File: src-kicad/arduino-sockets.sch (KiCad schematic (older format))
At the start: 48 parts, among them J10 1x8_female_pin_Header_2.54mm, J11 1x6_female_pin_Header_2.54mm, J12 1x6_male_pin_Header_2.54mm, J13 1x6_male_pin_Header_2.54mm, J14 1x6_male_pin_Header_2.54mm, J19 2x4_male_pin_Header_2.54mm, J2 1x6_male_pin_Header_2.54mm, J3 1x6_male_pin_Header_2.54mm, J4 1x10_female_pin_Header_2.54mm, J5 1x8_female_pin_Header_2.54mm, J6 1x6_male_pin_Header_2.54mm, J7 1x8_male_pin_Header_2.54mm, J8 1x8_male_pin_Header_2.54mm, J9 1x8_male_pin_Header_2.54mm, U6 TXB0106, U8 TXS0108, U9 TXB0108

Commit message: Kicad pcb migration: Sockets J10 and J4 added
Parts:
- J10, J5: footprint (none) -> Icezum:1x8_Socket_header_2.54mm
- J4: footprint (none) -> Icezum:1x10_socket-header-2.54mm
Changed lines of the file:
@@
 F 0 "J10" V 9400 2000 60  0000 C CNN
 F 1 "1x8_female_pin_Header_2.54mm" H 9600 850 60  0001 C CNN
-F 2 "" H 9250 1600 60  0000 C CNN
+F 2 "Icezum:1x8_Socket_header_2.54mm" H 9250 1600 60  0001 C CNN
 F 3 "" H 9250 1600 60  0000 C CNN
 	1    9250 1050
@@
 F 0 "J4" V 6200 2150 60  0000 C CNN
 F 1 "1x10_female_pin_Header_2.54mm" H 6220 860 60  0001 C CNN
-F 2 "" H 6050 1600 60  0000 C CNN
+F 2 "Icezum:1x10_socket-header-2.54mm" H 6050 1600 60  0001 C CNN
 F 3 "" H 6050 1600 60  0000 C CNN
 	1    6050 1050
@@
 F 0 "J5" V 5550 6700 60  0000 C CNN
 F 1 "1x8_female_pin_Header_2.54mm" H 5750 5600 60  0001 C CNN
-F 2 "" H 5400 6350 60  0000 C CNN
+F 2 "Icezum:1x8_Socket_header_2.54mm" H 5400 6350 60  0001 C CNN
 F 3 "" H 5400 6350 60  0000 C CNN
 	1    5400 5800
@@
 B8 D2 A5 D0 D0 88 43 83 08 6C BD D2 A5 D0 D0 88 C3 36 11 89 E7 80 EE 2B 5D 12 0D 8D 28 1C 42 E0
 0D 11 99 76 E0 6E E0 E3 2B 5D 22 0D 8D 71 EC 07 1E E7 1B 7C F8 FF 01 FB D1 C8 6E 4C 03 14 F4 00
-00 00 00 49 45 4E 44 AE 42 60 82 08
+00 00 00 49 45 4E 44 AE 42 60 82 65
 EndData
 $EndBitmap
@@
 F3 F0 1D 79 17 0B BC D0 AE 96 03 B8 3F 0C 6D B8 A2 A8 0B 16 2C 58 B0 60 C1 82 05 0B 16 2C 58 B0
 60 C1 82 05 0B 16 2C 58 B0 E0 7F 81 FF 00 64 C5 01 8A 14 5C 86 66 00 00 00 00 49 45 4E 44 AE 42
-60 82 00
+60 82 AB
 EndData
 $EndBitmap

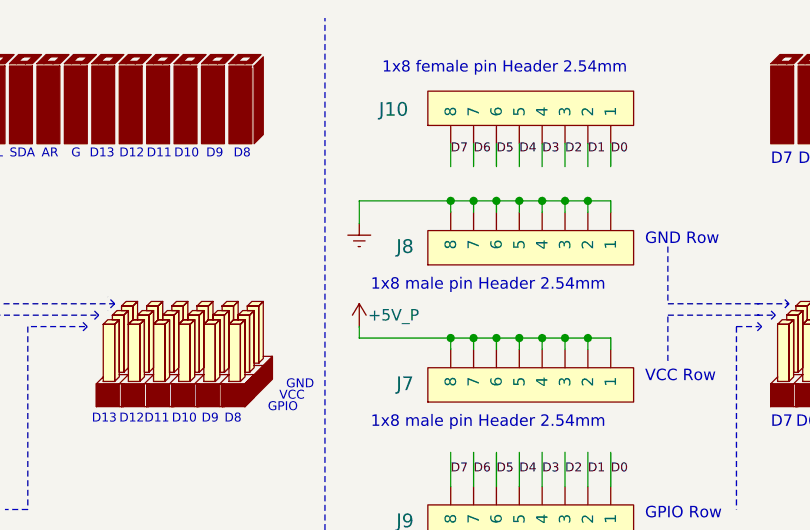
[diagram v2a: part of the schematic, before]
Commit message: Kicad pcb migration: J8 pin header added
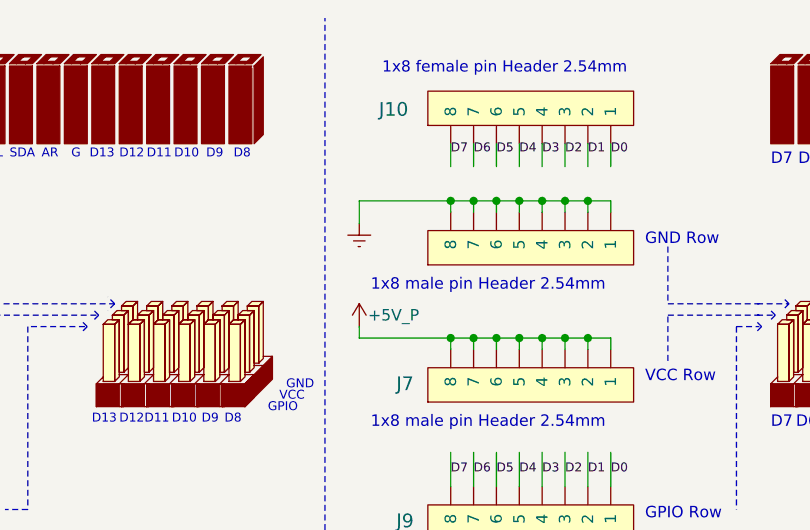
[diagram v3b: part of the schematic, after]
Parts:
- J7, J9: footprint (none) -> Icezum:1x8_Socket_header_2.54mm
- J8: footprint (none) -> Icezum:1x8_pin_header_2.54mm
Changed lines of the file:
@@
 U 1 1 57474AD5
 P 9250 1350
-F 0 "J8" V 9100 2250 60  0000 C CNN
+F 0 "J8" V 9100 2250 60  0001 C CNN
 F 1 "1x8_male_pin_Header_2.54mm" H 9000 1150 60  0001 C CNN
-F 2 "" H 9250 1900 60  0000 C CNN
+F 2 "Icezum:1x8_pin_header_2.54mm" H 9250 1900 60  0001 C CNN
 F 3 "" H 9250 1900 60  0000 C CNN
 	1    9250 1350
@@
 F 0 "J7" V 9100 2850 60  0000 C CNN
 F 1 "1x8_male_pin_Header_2.54mm" H 9140 1760 60  0001 C CNN
-F 2 "" H 9250 2500 60  0000 C CNN
+F 2 "Icezum:1x8_Socket_header_2.54mm" H 9250 2500 60  0001 C CNN
 F 3 "" H 9250 2500 60  0000 C CNN
 	1    9250 1950
@@
 F 0 "J9" V 9100 3450 60  0000 C CNN
 F 1 "1x8_male_pin_Header_2.54mm" H 9140 2360 60  0001 C CNN
-F 2 "" H 9250 3100 60  0000 C CNN
+F 2 "Icezum:1x8_Socket_header_2.54mm" H 9250 3100 60  0001 C CNN
 F 3 "" H 9250 3100 60  0000 C CNN
 	1    9250 2550
@@
 B8 D2 A5 D0 D0 88 43 83 08 6C BD D2 A5 D0 D0 88 C3 36 11 89 E7 80 EE 2B 5D 12 0D 8D 28 1C 42 E0
 0D 11 99 76 E0 6E E0 E3 2B 5D 22 0D 8D 71 EC 07 1E E7 1B 7C F8 FF 01 FB D1 C8 6E 4C 03 14 F4 00
-00 00 00 49 45 4E 44 AE 42 60 82 65
+00 00 00 49 45 4E 44 AE 42 60 82 00
 EndData
 $EndBitmap
@@
 F3 F0 1D 79 17 0B BC D0 AE 96 03 B8 3F 0C 6D B8 A2 A8 0B 16 2C 58 B0 60 C1 82 05 0B 16 2C 58 B0
 60 C1 82 05 0B 16 2C 58 B0 E0 7F 81 FF 00 64 C5 01 8A 14 5C 86 66 00 00 00 00 49 45 4E 44 AE 42
-60 82 AB
+60 82 40
 EndData
 $EndBitmap

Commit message: Kicad pcb migration: Some sockets and header added
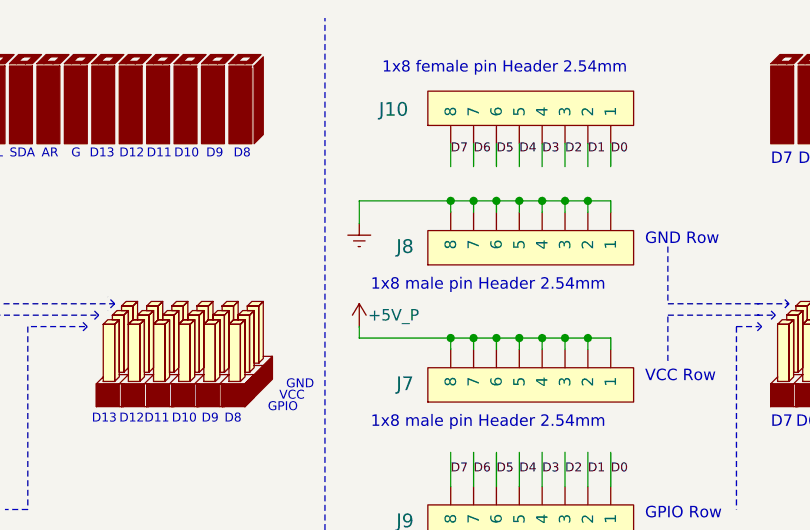
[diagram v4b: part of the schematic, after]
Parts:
- J11: footprint (none) -> Icezum:1x6-Socket-header-2.54mm
- J7, J9: footprint Icezum:1x8_Socket_header_2.54mm -> Icezum:1x8_pin_header_2.54mm
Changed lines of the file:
@@
 U 1 1 57474AD5
 P 9250 1350
-F 0 "J8" V 9100 2250 60  0001 C CNN
+F 0 "J8" V 9100 2250 60  0000 C CNN
 F 1 "1x8_male_pin_Header_2.54mm" H 9000 1150 60  0001 C CNN
 F 2 "Icezum:1x8_pin_header_2.54mm" H 9250 1900 60  0001 C CNN
@@
 F 0 "J7" V 9100 2850 60  0000 C CNN
 F 1 "1x8_male_pin_Header_2.54mm" H 9140 1760 60  0001 C CNN
-F 2 "Icezum:1x8_Socket_header_2.54mm" H 9250 2500 60  0001 C CNN
+F 2 "Icezum:1x8_pin_header_2.54mm" H 9250 2500 60  0001 C CNN
 F 3 "" H 9250 2500 60  0000 C CNN
 	1    9250 1950
@@
 F 0 "J9" V 9100 3450 60  0000 C CNN
 F 1 "1x8_male_pin_Header_2.54mm" H 9140 2360 60  0001 C CNN
-F 2 "Icezum:1x8_Socket_header_2.54mm" H 9250 3100 60  0001 C CNN
+F 2 "Icezum:1x8_pin_header_2.54mm" H 9250 3100 60  0001 C CNN
 F 3 "" H 9250 3100 60  0000 C CNN
 	1    9250 2550
@@
 F 0 "J11" V 8950 5950 60  0000 C CNN
 F 1 "1x6_female_pin_Header_2.54mm" H 8920 5960 60  0001 C CNN
-F 2 "" H 8750 6700 60  0000 C CNN
+F 2 "Icezum:1x6-Socket-header-2.54mm" H 8750 6700 60  0001 C CNN
 F 3 "" H 8750 6700 60  0000 C CNN
 	1    8750 6150
@@
 F3 F0 1D 79 17 0B BC D0 AE 96 03 B8 3F 0C 6D B8 A2 A8 0B 16 2C 58 B0 60 C1 82 05 0B 16 2C 58 B0
 60 C1 82 05 0B 16 2C 58 B0 E0 7F 81 FF 00 64 C5 01 8A 14 5C 86 66 00 00 00 00 49 45 4E 44 AE 42
-60 82 40
+60 82 00
 EndData
 $EndBitmap

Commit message: Kicad pcb migration: I/O pin header connectors placed
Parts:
- J12, J13, J14, J2, J3, J6: footprint (none) -> Icezum:1x6-pin-header-2.54mm
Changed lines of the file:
@@
 F 0 "J3" V 5850 2050 60  0000 C CNN
 F 1 "1x6_male_pin_Header_2.54mm" H 5940 1160 60  0001 C CNN
-F 2 "" H 6050 1900 60  0000 C CNN
+F 2 "Icezum:1x6-pin-header-2.54mm" H 6050 1900 60  0001 C CNN
 F 3 "" H 6050 1900 60  0000 C CNN
 	1    6050 1350
@@
 F 0 "J2" V 5850 2650 60  0000 C CNN
 F 1 "1x6_male_pin_Header_2.54mm" H 5940 1760 60  0001 C CNN
-F 2 "" H 6050 2500 60  0000 C CNN
+F 2 "Icezum:1x6-pin-header-2.54mm" H 6050 2500 60  0001 C CNN
 F 3 "" H 6050 2500 60  0000 C CNN
 	1    6050 1950
@@
 F 0 "J6" V 5850 3250 60  0000 C CNN
 F 1 "1x6_male_pin_Header_2.54mm" H 5940 2360 60  0001 C CNN
-F 2 "" H 6050 3100 60  0000 C CNN
+F 2 "Icezum:1x6-pin-header-2.54mm" H 6050 3100 60  0001 C CNN
 F 3 "" H 6050 3100 60  0000 C CNN
 	1    6050 2550
@@
 F 0 "J12" V 8600 4250 60  0000 C CNN
 F 1 "1x6_male_pin_Header_2.54mm" H 8640 4260 60  0001 C CNN
-F 2 "" H 8750 5000 60  0000 C CNN
+F 2 "Icezum:1x6-pin-header-2.54mm" H 8750 5000 60  0001 C CNN
 F 3 "" H 8750 5000 60  0000 C CNN
 	1    8750 4450
@@
 F 0 "J13" V 8550 4850 60  0000 C CNN
 F 1 "1x6_male_pin_Header_2.54mm" H 8640 4860 60  0001 C CNN
-F 2 "" H 8750 5600 60  0000 C CNN
+F 2 "Icezum:1x6-pin-header-2.54mm" H 8750 5600 60  0001 C CNN
 F 3 "" H 8750 5600 60  0000 C CNN
 	1    8750 5050
@@
 F 0 "J14" V 8550 5350 60  0000 C CNN
 F 1 "1x6_male_pin_Header_2.54mm" H 8640 5360 60  0001 C CNN
-F 2 "" H 8750 6100 60  0000 C CNN
+F 2 "Icezum:1x6-pin-header-2.54mm" H 8750 6100 60  0001 C CNN
 F 3 "" H 8750 6100 60  0000 C CNN
 	1    8750 5550
@@
 B8 D2 A5 D0 D0 88 43 83 08 6C BD D2 A5 D0 D0 88 C3 36 11 89 E7 80 EE 2B 5D 12 0D 8D 28 1C 42 E0
 0D 11 99 76 E0 6E E0 E3 2B 5D 22 0D 8D 71 EC 07 1E E7 1B 7C F8 FF 01 FB D1 C8 6E 4C 03 14 F4 00
-00 00 00 49 45 4E 44 AE 42 60 82 00
+00 00 00 49 45 4E 44 AE 42 60 82 05
 EndData
 $EndBitmap

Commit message: Kicad pcb migration: Pin headers J15, J16, J17 and J19 added
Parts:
- J19: footprint (none) -> Icezum:2x04-pin-header-2.54mm
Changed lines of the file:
@@
 F 0 "J19" V 5300 4350 60  0000 C CNN
 F 1 "2x4_male_pin_Header_2.54mm" H 5350 3690 60  0001 C CNN
-F 2 "" H 4900 4200 60  0000 C CNN
+F 2 "Icezum:2x04-pin-header-2.54mm" H 4900 4200 60  0001 C CNN
 F 3 "" H 4900 4200 60  0000 C CNN
 	1    5050 4150
